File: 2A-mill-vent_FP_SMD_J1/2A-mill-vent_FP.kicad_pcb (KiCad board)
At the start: 2 copper layers, 53.8 x 30.5 mm, 16 parts, among them J1 Front_panel_control, J2 Conn_01x02_Male, SW1 Fan_Down, SW2 Fan_Up, SW3 Power_On, SW4 Power_off

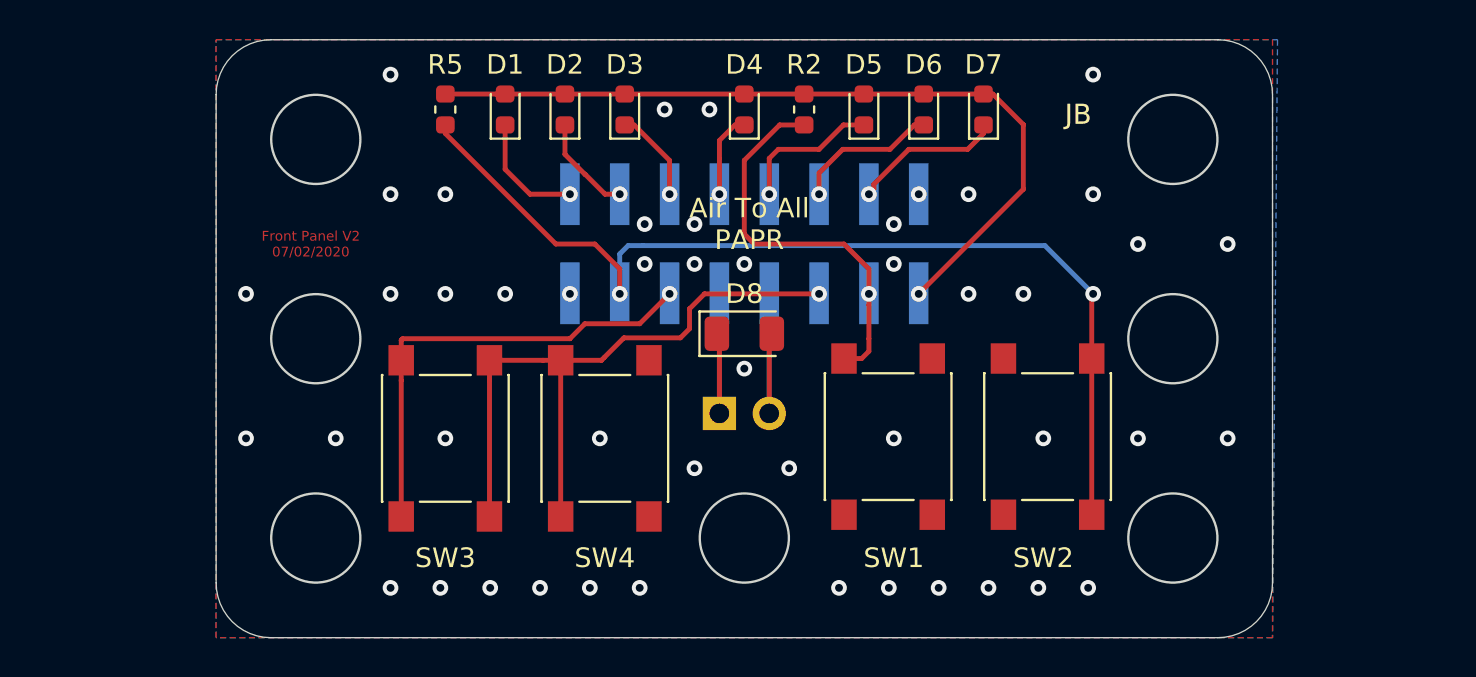
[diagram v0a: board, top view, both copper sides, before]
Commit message: Made major changes to 2A and started an all in one board
2A is a longer SMD front panel board now, no plans on updating 2b. work on 1, 2 , 2A, 2B has stoped.
Now looking at 3 to cut cost greatly with not having to interconnect two boards and make two boards. just the parts cost savings is in the order of $30 in qty1
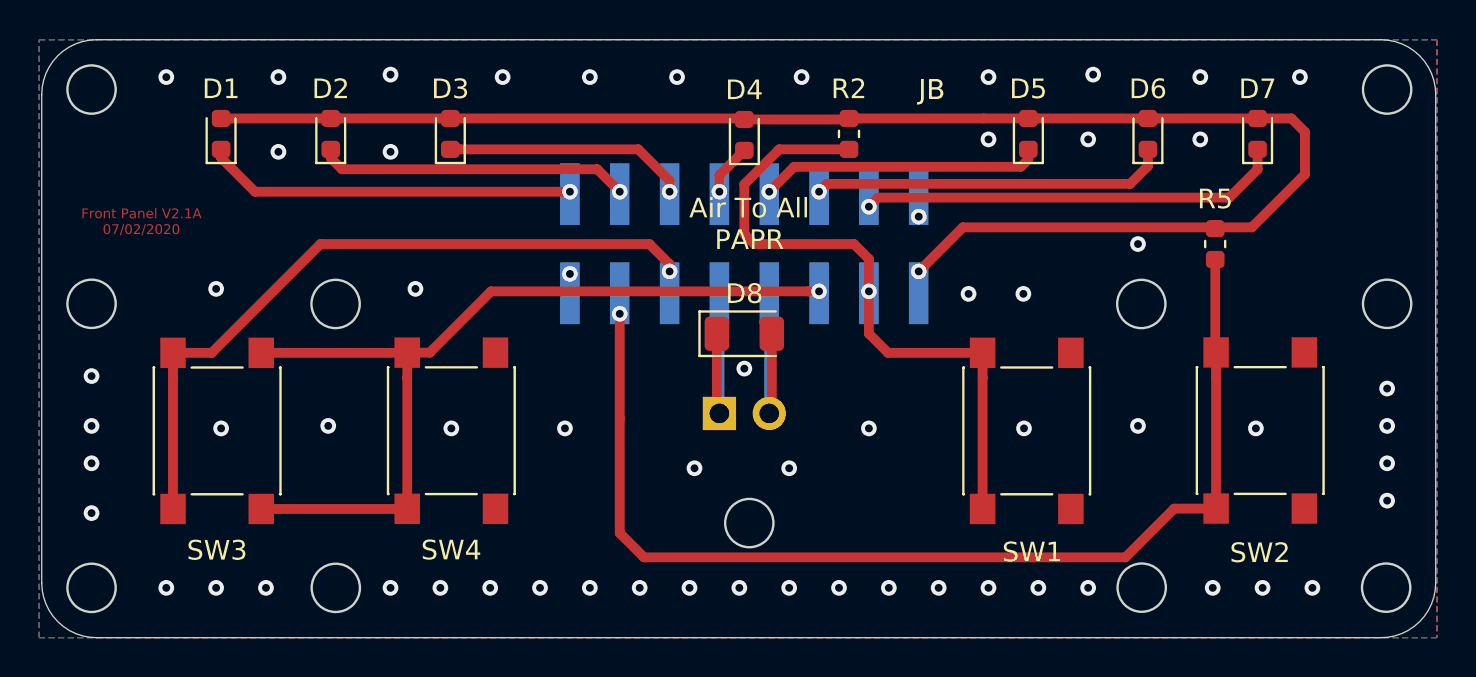
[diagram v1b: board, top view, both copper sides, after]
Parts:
- moved R5 39.8 mm to (214.8, 61.2)
- moved D1 14.5 mm to (164.1, 55.6)
- moved D7 14.0 mm to (216.9, 55.6)
- moved D2 12.0 mm to (169.7, 55.6)
- moved SW3 11.6 mm to (163.9, 70.7)
- moved D6 11.5 mm to (211.3, 55.6)
- moved SW2 10.8 mm to (217.1, 70.7), turned to 270 degrees
- moved D3 8.98 mm to (175.8, 55.6)
- moved D5 8.47 mm to (205.2, 55.6)
- moved SW4 7.83 mm to (175.8, 70.7)
- moved SW1 7.07 mm to (205.2, 70.7)
- moved R2 2.60 mm to (196.1, 55.6)
- moved D4 1.30 mm to (190.8, 55.7)
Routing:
- net +5V: track 40.9 -> 79.5 mm
- net LED7: track 7.71 -> 21.6 mm
- net Down: track 20.3 -> 33.5 mm
- net LED1: track 6.09 -> 18.9 mm
- net ON: track 23.6 -> 36.4 mm
- net LED2: track 5.13 -> 15.9 mm
- net LED6: track 7.43 -> 18.2 mm
- net ON\*OFF: track 34.7 -> 45.1 mm
- net LED3: track 4.76 -> 12.4 mm
- net LED5: track 7.36 -> 14.4 mm
- net Up: track 52.3 -> 56.6 mm, vias 2 -> 1
- net LED4: track 4.33 -> 2.63 mm
- net Motor+: track 11.5 -> 10.3 mm
- net GND: vias 48 -> 63
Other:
- board size 53.8 x 30.5 mm -> 71.1 x 30.5 mm
- board text added: "Front Panel V2.1A 07/02/2020"
- board text removed: "Front Panel V2 07/02/2020"
